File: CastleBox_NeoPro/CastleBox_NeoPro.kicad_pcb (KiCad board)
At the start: 4 copper layers, 74 x 48 mm, 107 parts, among them J1 USB_RP2350A, J2 USB_FPGA, J3 USB_A, J4 USB_A, J5 HDMI_A, J6 Conn_02x20_Odd_Even, SW1 SW_Push, U1 EA3036, U2 XC6SLX9-FTG256, U3 RP2350_60QFN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

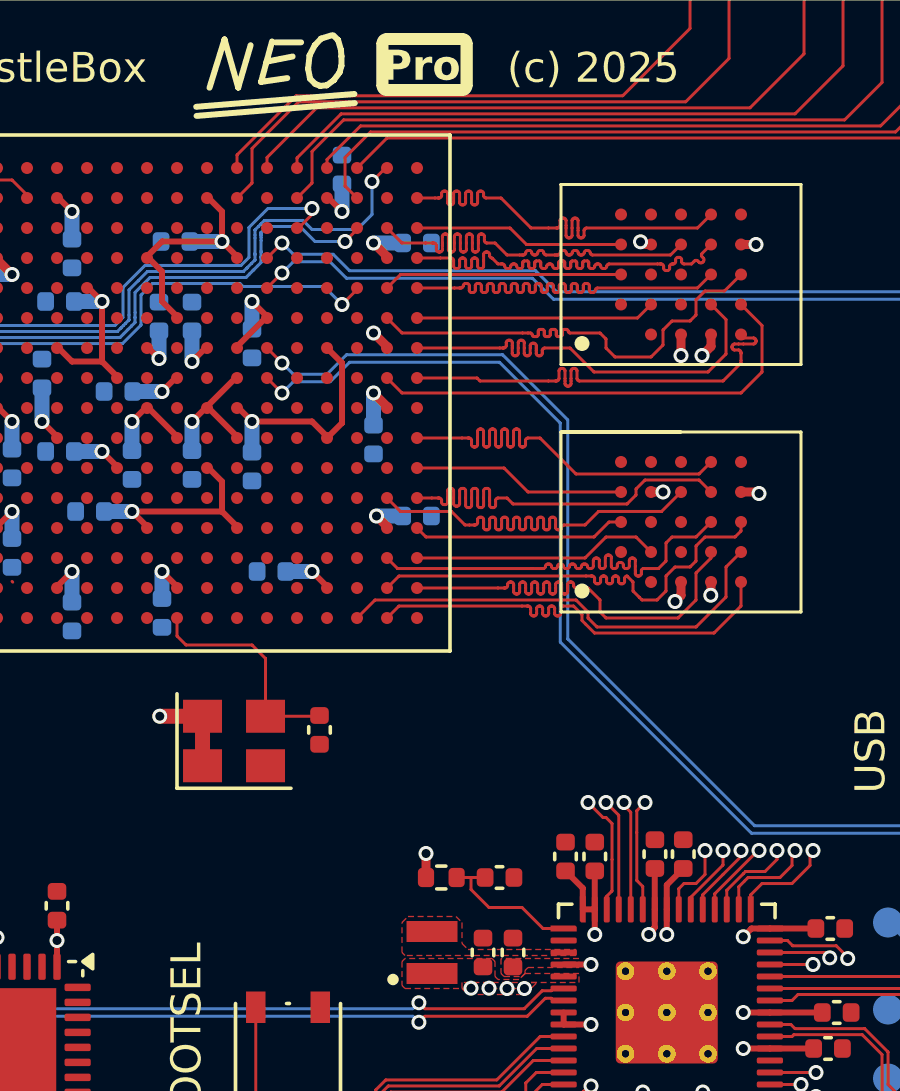
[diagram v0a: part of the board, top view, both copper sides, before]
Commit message: added SPI communication protocol
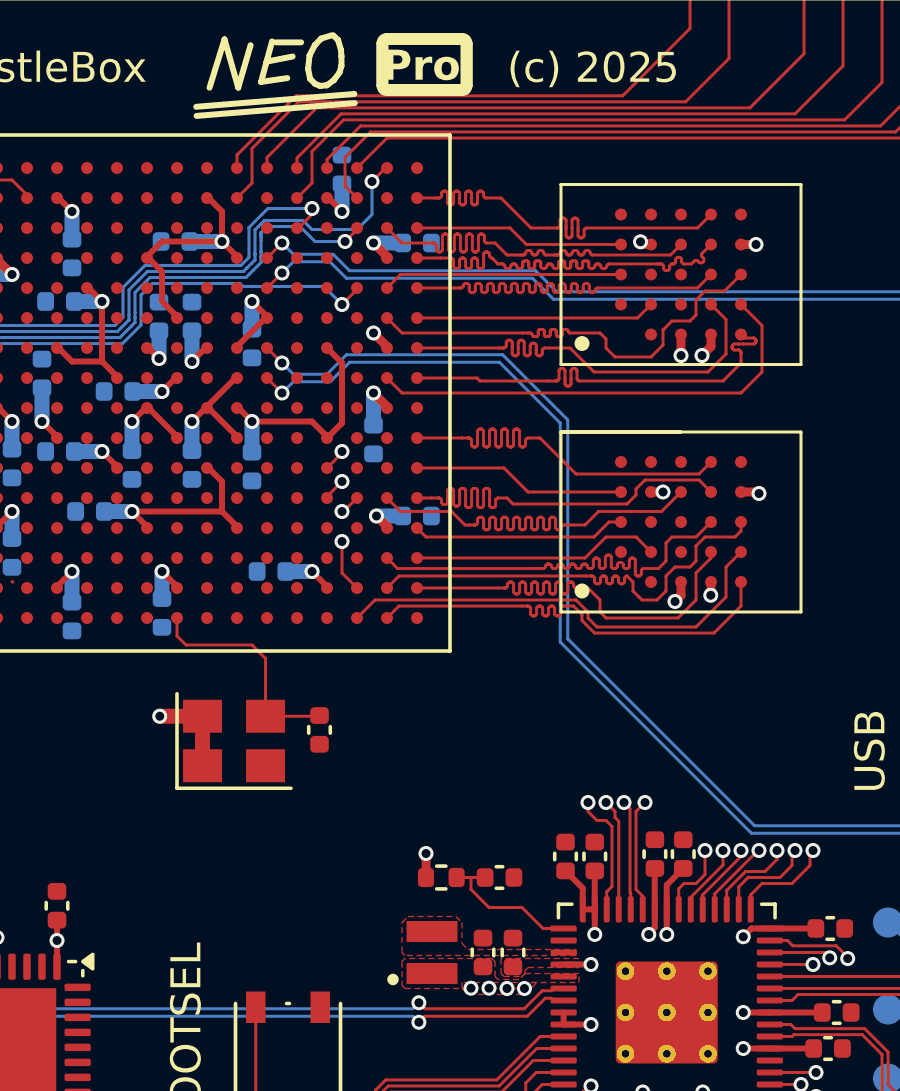
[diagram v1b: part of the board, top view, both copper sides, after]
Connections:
- J6 pad 3: /Microcontroller/P29 -> FPGA_CS
- J6 pad 5: /Microcontroller/P28 -> FPGA_MISO
- J6 pad 7: /Microcontroller/P26 -> FPGA_SCK
- J6 pad 8: /Microcontroller/P27 -> FPGA_MOSI
- U2 pad L13: unconnected-(U2A-IO_L53N_VREF_1-PadL13) -> FPGA_CS
- U2 pad M13: unconnected-(U2A-IO_L74P_AWAKE_1-PadM13) -> FPGA_MISO
- U2 pad M14: unconnected-(U2A-IO_L74N_DOUT_BUSY_1-PadM14) -> FPGA_MOSI
- U2 pad R14: unconnected-(U2A-IO_L50P_M1UDQS_1-PadR14) -> FPGA_SCK
- U3 pad 40: /Microcontroller/P26 -> FPGA_SCK
- U3 pad 41: /Microcontroller/P27 -> FPGA_MOSI
- U3 pad 42: /Microcontroller/P28 -> FPGA_MISO
- U3 pad 43: /Microcontroller/P29 -> FPGA_CS
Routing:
- net FPGA_MOSI: track 0.00 -> 81.5 mm, vias 0 -> 2
- net FPGA_CS: track 0.00 -> 81.0 mm, vias 0 -> 2
- net FPGA_MISO: track 0.00 -> 79.1 mm, vias 0 -> 2
- net FPGA_SCK: track 0.00 -> 78.3 mm, vias 0 -> 2
- net /Microcontroller/P29: track 59.0 -> 0.00 mm, vias 1 -> 0
- net /Microcontroller/P27: track 58.9 -> 0.00 mm, vias 1 -> 0
- net /Microcontroller/P28: track 56.7 -> 0.00 mm, vias 1 -> 0
- net /Microcontroller/P26: track 55.1 -> 0.00 mm, vias 1 -> 0
- net +1V1: track 27.1 -> 31.0 mm
